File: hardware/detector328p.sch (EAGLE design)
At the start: 40 parts, among them J2 AVR_SPI_PRG_6NS, Q2 16MHz, T1 BC337, T3 BC337, U2 TINY85-20-DIP

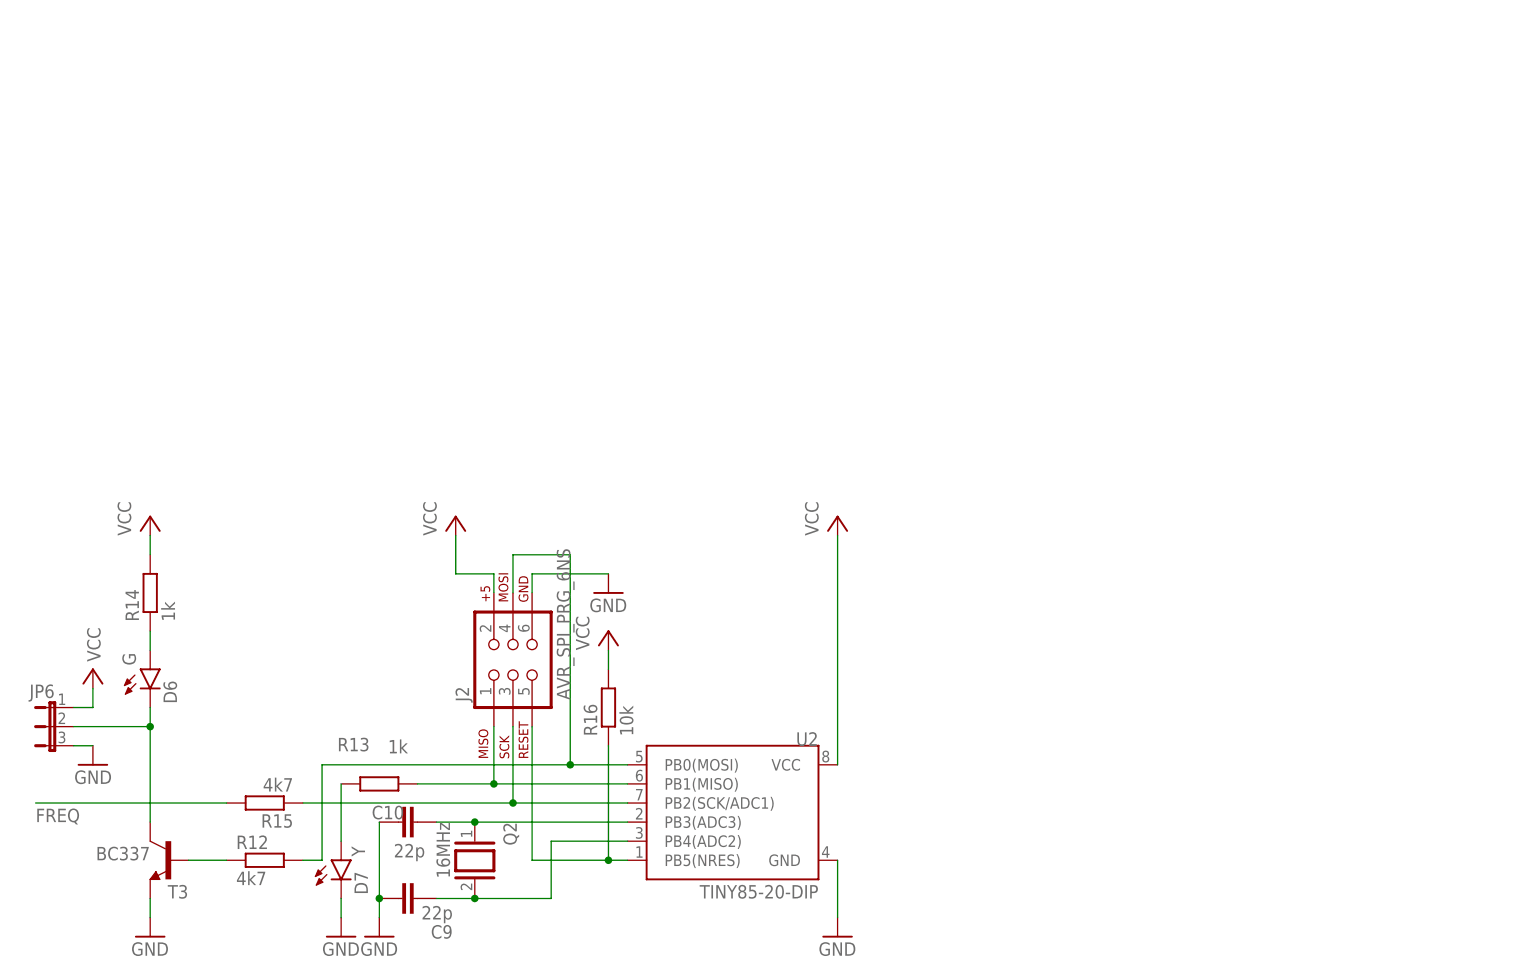
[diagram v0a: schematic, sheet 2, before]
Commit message: hardware: separate pages for analog and digital part, separate schematics for tiny85 and mega328p
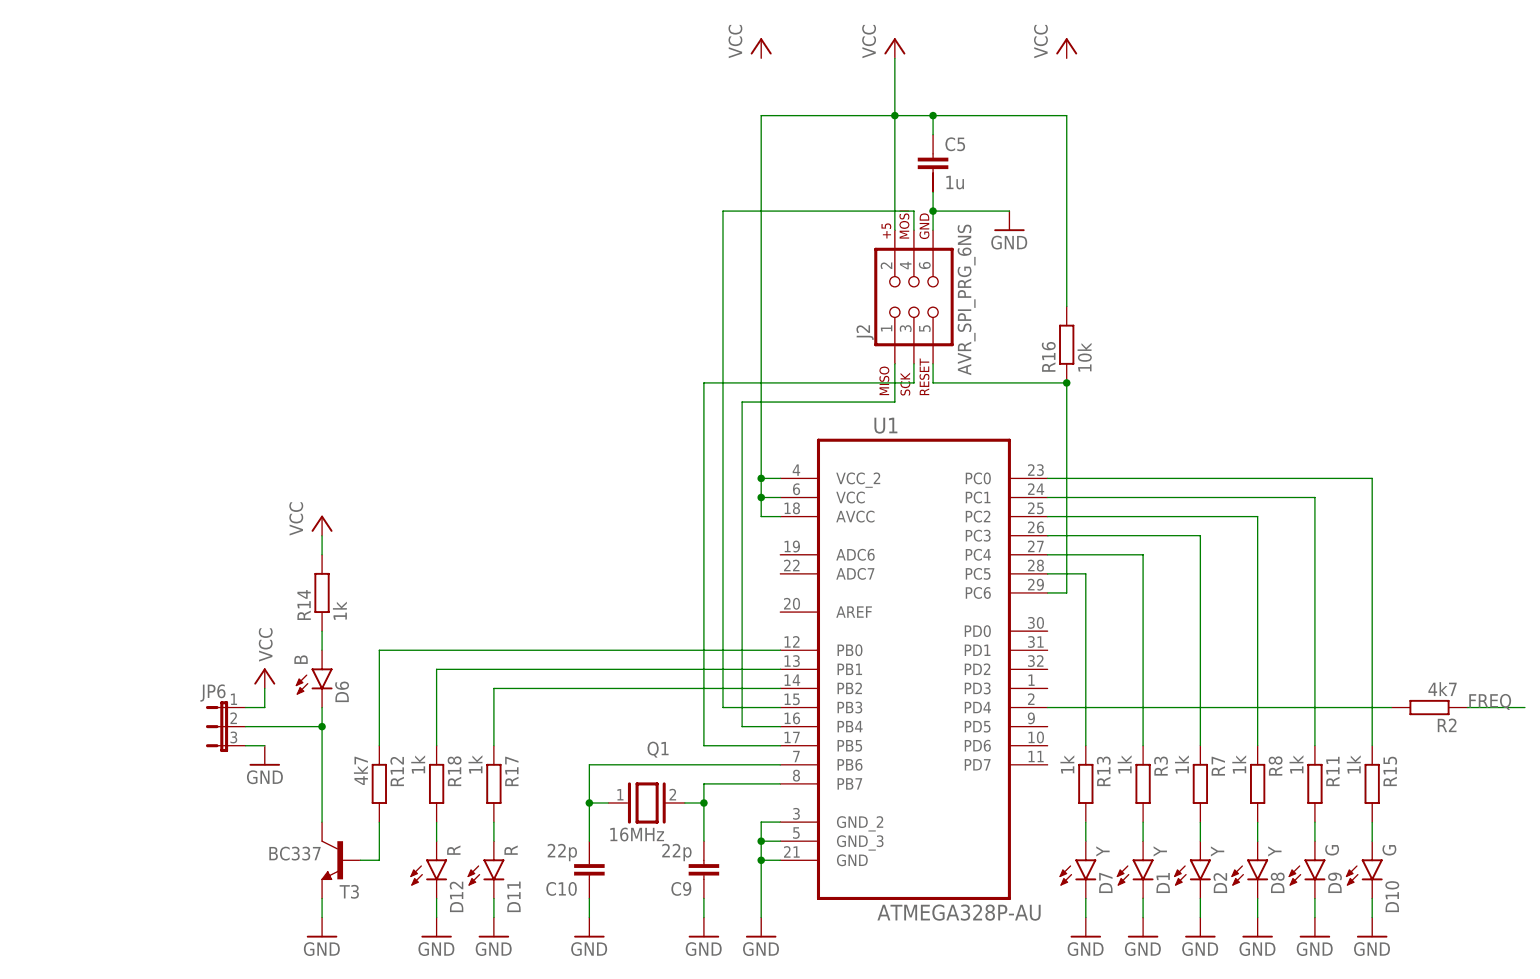
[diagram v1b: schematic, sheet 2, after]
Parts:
- removed Q2: 16MHz, special:XTAL/S
- removed U2: TINY85-20-DIP, SparkFun-DigitalIC:ATTINY45TINY45-20-DIP
- added C5: 1u, capacitor-wima:C-2.5-5/4
- added D1, D2, D8: Y, SparkFun-LED:LED3MM
- added D10, D9: G, SparkFun-LED:LED3MM
- added D11, D12: R, SparkFun-LED:LED3MM
- added Q1: 16MHz, special:XTAL/S
- added R11, R17, R18, R3, R7, R8: 1k, resistor:R-EU_0204/5
- added R2: 4k7, resistor:R-EU_0204/5
- added U1: ATMEGA328P-AU, Atmel_By_element14_Batch_1-00:ATMEGA328P-AU
- D6: value G -> B
- R15: value 4k7 -> 1k
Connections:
- new net N$10: C9.2, Q1.2, U1.PB7
- new net N$12: J2.1, U1.PB4
- new net N$13: J2.4, U1.PB3
- new net N$15: J2.3, U1.PB5
- new net N$16: D1.A, R3.2
- new net N$17: D2.A, R7.2
- new net N$18: D8.A, R8.2
- new net N$19: D9.A, R11.2
- new net N$32: D10.A, R15.2
- new net N$33: R15.1, U1.PC0
- new net N$34: D11.A, R17.2
- new net N$35: D12.A, R18.2
- new net N$36: R17.1, U1.PB2
- new net N$37: R18.1, U1.PB1
- new net N$38: R12.1, U1.PB0
- new net N$8: C10.2, Q1.1, U1.PB6
- new net N$9: R2.2, U1.PD4
- net FREQ: now also R2.1; no longer R15.2
- net GND: now also C5.2, D1.C, D10.C, D11.C, D12.C, D2.C, D8.C, D9.C, U1.GND, U1.GND_2, U1.GND_3; no longer U2.GND
- net N$20: now also R12.2; no longer R12.1
- net N$25: now also R13.1, U1.PC5; no longer C10.2, Q2.1, U2.PB3(ADC3)
- net N$26: now also R3.1, U1.PC4; no longer C9.2, Q2.2, U2.PB4(ADC2)
- net N$28: now also R7.1, U1.PC3; no longer J2.1, R13.1, U2.PB1(MISO)
- net N$29: now also R8.1, U1.PC2; no longer J2.4, R12.2, U2.PB0(MOSI)
- net N$30: now also U1.PC6; no longer U2.PB5(NRES)
- net N$31: now also R11.1, U1.PC1; no longer J2.3, R15.1, U2.PB2(SCK/ADC1)
- net VCC: now also C5.1, U1.AVCC, U1.VCC, U1.VCC_2; no longer U2.VCC
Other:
- moved on the sheet: C10, C9, D6, D7, J2, JP6, R12, R13, R14, R15, R16, T3
